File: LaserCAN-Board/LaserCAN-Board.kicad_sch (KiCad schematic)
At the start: 49 parts, among them J2 TC2050-IDC-NL, U1 NCP730BMT330TBG, U10 M24C64-RMN6TP, U2 VL53L1CXV0FY1, U4 STM32F103C8Tx, U9 SN65HVD230, U9 TPS54202DDC

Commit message: Rev 4 updates
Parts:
- removed D4, D5: PESD1CAN,215, PESD1CAN:SOT-23_L2.9-W1.3-P1.90-LS2.4-BR, symbol PESD1CAN:PESD1CAN,215
- removed R1, R5: 10k, Resistor_SMD:R_0402_1005Metric, symbol Device:R
- removed R3, R4: 4k7, Resistor_SMD:R_0402_1005Metric, symbol Device:R
- removed U1: NCP730BMT330TBG, NCP730BMT330TBG:WDFN-6_L2.0-W2.0-P0.65-BL-EP-1, symbol NCP730BMT330TBG:NCP730BMT330TBG
- added C10, C11: 22uF, Capacitor_SMD:C_0603_1608Metric, symbol Device:C_Small
- added C14, C15: 100n, Capacitor_SMD:C_0402_1005Metric, symbol Device:C_Small
- added D4: ESDCAN24-2BLY, Package_TO_SOT_SMD:SOT-23, symbol Power_Protection:SZNUP2105L
- added D6: SMF12A, Diode_SMD:D_SOD-123F, symbol Diode:SMF12A
- added NT1: NetTie_2, NetTie:NetTie-2_SMD_Pad0.5mm, symbol Device:NetTie_2
- added NT2: NetTie_2, NetTie:NetTie-2_SMD_Pad2.0mm, symbol Device:NetTie_2
- added RN1: YC164-JR-074K7L, Resistor_SMD:R_Array_Convex_4x0603, symbol Device:R_Pack04
- added U1: TPS7A2033PDBVR, Package_TO_SOT_SMD:SOT-23-5, symbol Regulator_Linear:TPS7A0508PDBV
- C19: value 22uF -> 10uF; footprint Capacitor_SMD:C_0805_2012Metric -> Capacitor_SMD:C_0603_1608Metric; LCSC Part C45783 -> C96446
- D1: value SS14 -> ZLLS400TA; footprint Diode_SMD:D_SMA -> Diode_SMD:D_SOD-323; LCSC Part C2480 -> C460267
- R9: LCSC Part C23164 -> C3009058
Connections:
- net +12V: now also D6.1 (A1)
- net +3V3: now also C19.1, C14.1, C15.1, RN1.5 (R4.2), RN1.6 (R3.2), RN1.7 (R2.2), RN1.8 (R1.2), U1.5 (OUT)
- net 3V87: now also C10.1, C11.1, U1.1 (IN), U1.3 (EN); no longer C19.1
- net CANH: now also D4.1 (K)
- net CANL: now also D4.2 (K)
- net GND: now also C10.2, C11.2, C14.2, C15.2, D4.3 (A), D6.2 (A2), NT1.2, NT2.1, U1.2 (GND); no longer J4.1, J5.1, R8.2
- net I2C_SCL: now also RN1.2 (R2.1)
- net I2C_SDA: now also RN1.1 (R1.1)
- net TOF_INT: now also RN1.3 (R3.1)
- net TOF_SHUT: now also RN1.4 (R4.1)
- new net: NT1.1, R8.2
- new net GNDPWR: J4.1, J5.1, NT2.2
- no-connect marks 34 -> 33
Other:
- note added: "CRCW06034R70JNEAHP for pulse"
- note added: "ESD Protection Diode"

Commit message: Rev 4 - more updates
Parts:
- added C20, C21: 33pF, Capacitor_SMD:C_0402_1005Metric, symbol Device:C_Small
- added Y1: 8MHz 20pF, Crystal:Crystal_SMD_3225-4Pin_3.2x2.5mm, symbol Device:Crystal_GND24_Small
- D6: value SMF12A -> SMF15CA; footprint Diode_SMD:D_SOD-123F -> Diode_SMD:D_SMF; symbol Diode:SMF12A -> Device:D_TVS; LCSC Part (none) -> C726952
- U1: LCSC Part (none) -> C2862740
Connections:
- net GND: now also C20.1, C21.1, Y1.2, Y1.4
- net at U4.5 (PD0): now also C21.2, Y1.3
- net at U4.6 (PD1): now also C20.2, Y1.1
- no-connect marks 33 -> 31
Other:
- moved on the sheet: C4, R10

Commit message: Rev 4 Complete, barring any more review
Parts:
- removed D1: ZLLS400TA, Diode_SMD:D_SOD-323, symbol Device:D_Schottky
- added D1: 12V, Diode_SMD:D_SOD-523, symbol Device:D_Zener_Small
- added Q1: Si2309CDS-T1-GE3, SI2309CDS-T1-GE3:SOT-23_L2.9-W1.3-P1.90-LS2.4-BR, symbol SI2309CDS-T1-GE3:Si2309CDS-T1-GE3
- added R1: 10k, Resistor_SMD:R_0402_1005Metric, symbol Device:R_US
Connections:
- net +12V: now also Q1.3 (D)
- net GND: now also U4.4 (PC15), R1.1
- net at R9.1: now also D1.1 (K), Q1.2 (S)
- new net: D1.2 (A), Q1.1 (G), R1.2
- no-connect marks 31 -> 30
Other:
- moved on the sheet: D6, FB1, R9

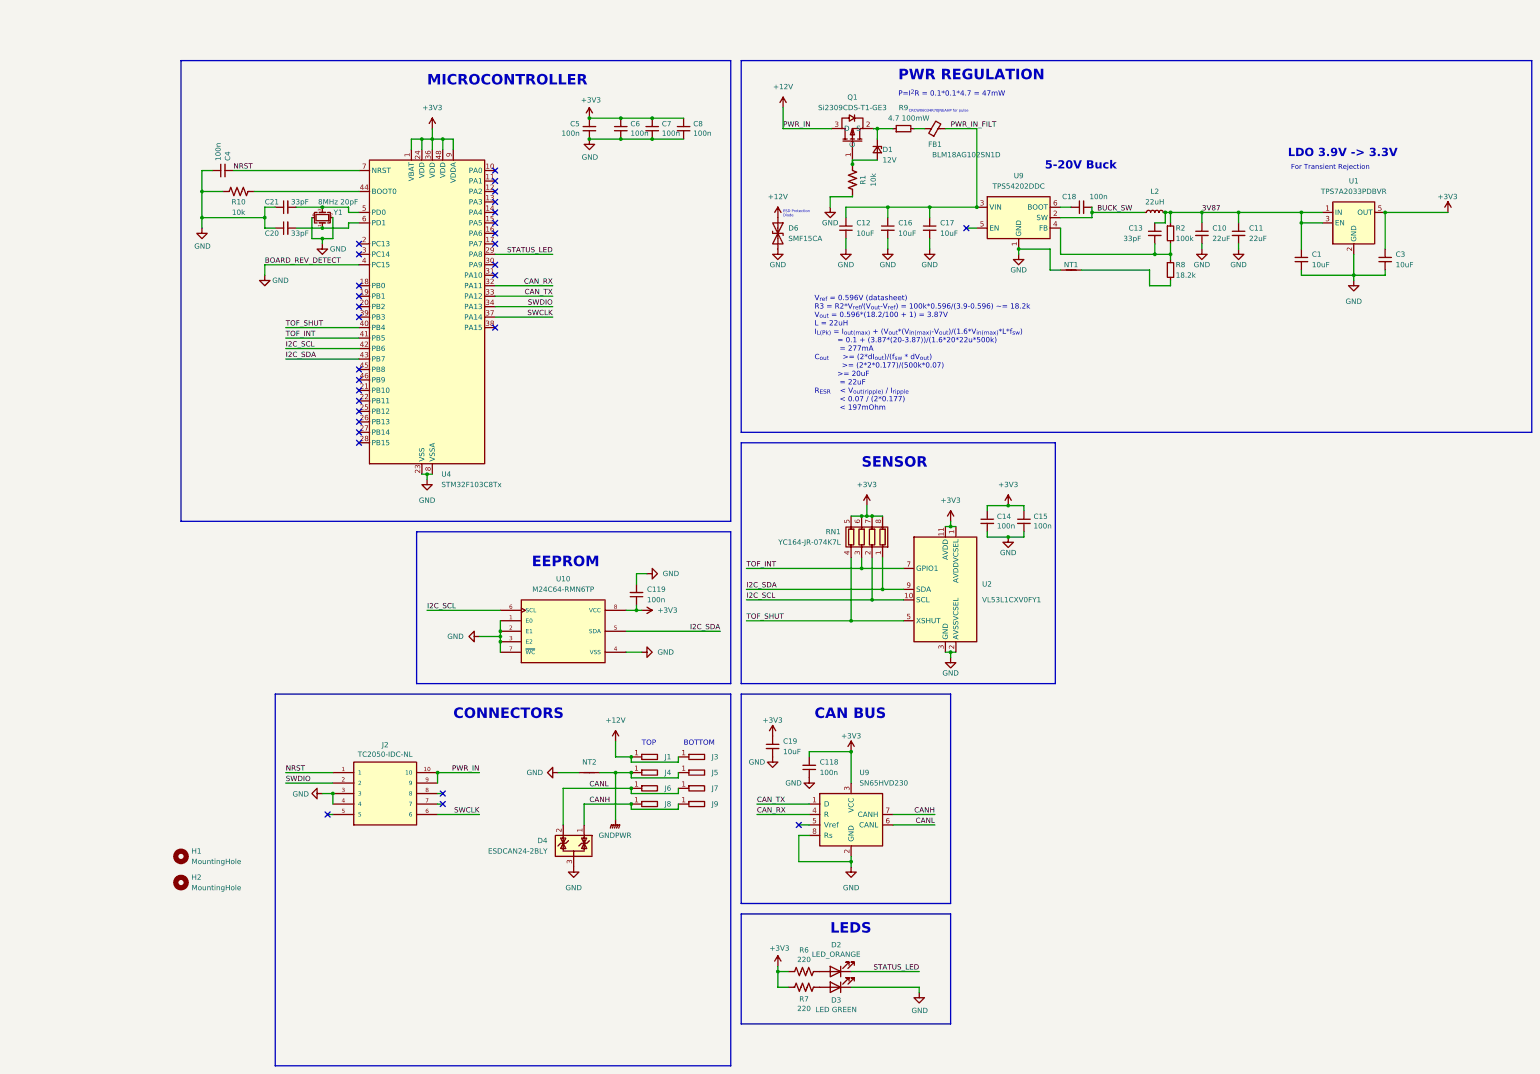
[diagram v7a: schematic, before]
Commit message: Rev 4 updates - NPTH, improved routing, BOM optimisation
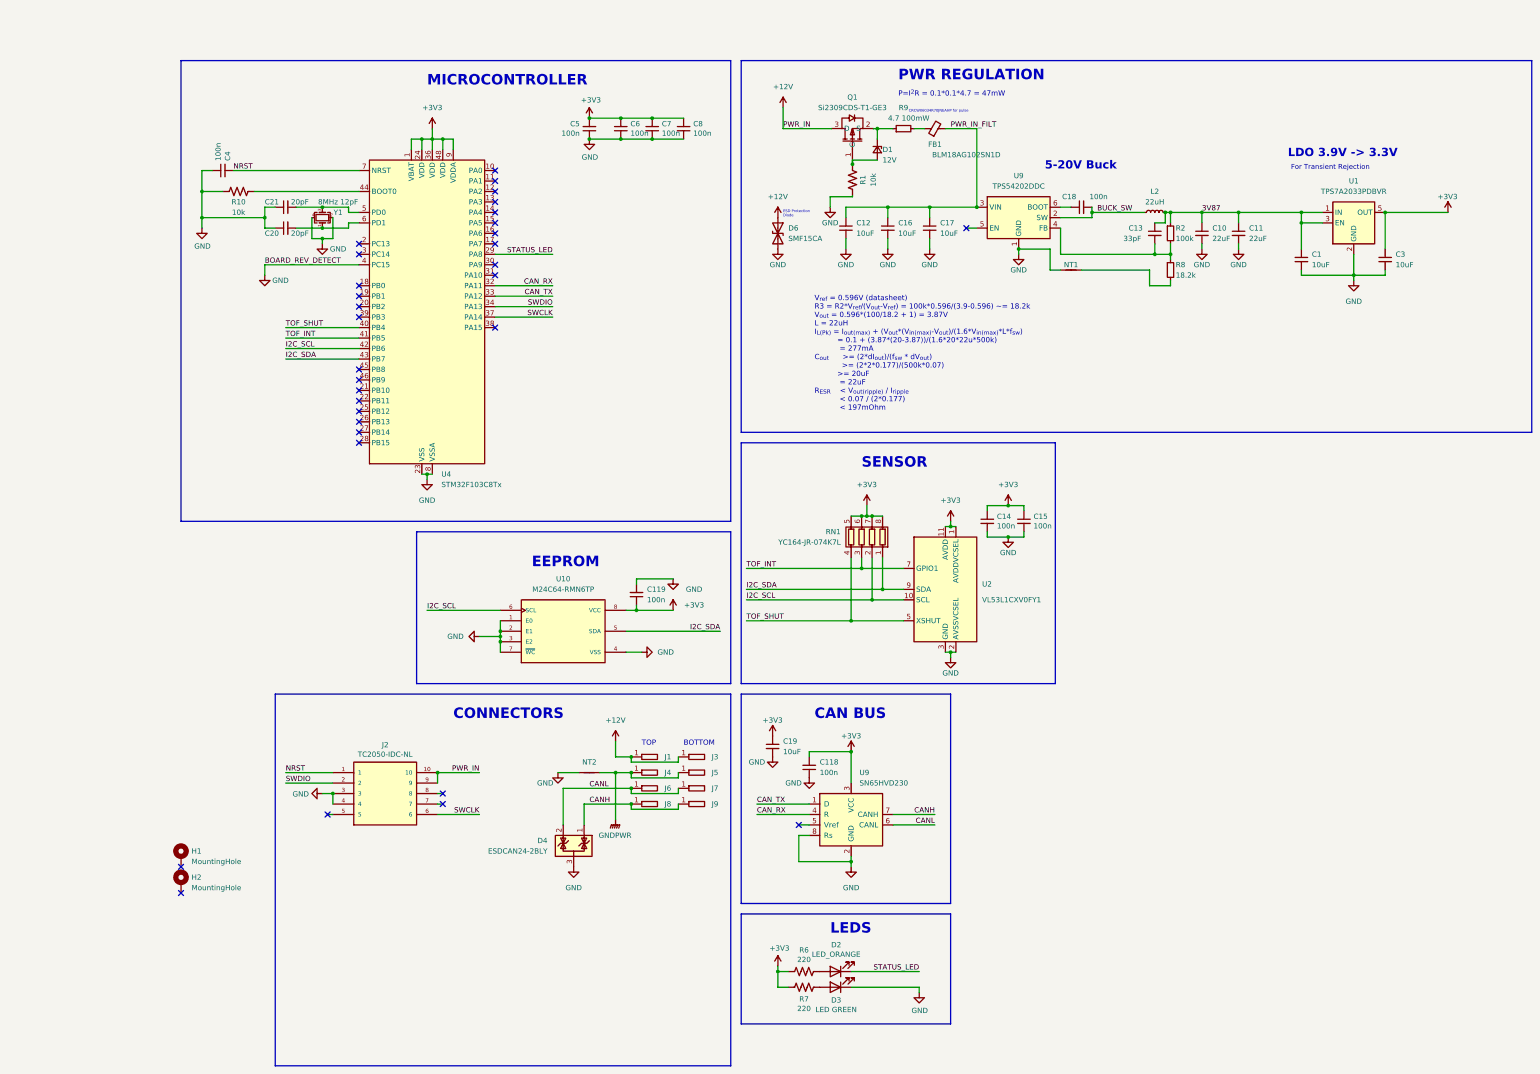
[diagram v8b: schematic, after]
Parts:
- C20, C21: value 33pF -> 20pF; LCSC Part C1562 -> C1554
- D1: LCSC C131801 -> (none); LCSC Part (none) -> C131801
- H1, H2: footprint MountingHole:MountingHole_3.2mm_M3 -> MountingHole:MountingHole_3.2mm_M3_Pad_TopBottom; symbol Mechanical:MountingHole -> Mechanical:MountingHole_Pad
- Y1: value 8MHz 20pF -> 8MHz 12pF
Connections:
- no-connect marks 30 -> 32
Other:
- note added: "V_{ref} = 0.596V (datasheet) R3 = R2*V_{ref}/(V_{out}-V_{ref}) = 100k*0.596/(3.9-0.596) ~= 18.2k V_{out} = 0.596*(100/18.2 + 1) = 3.87V L = 22uH I_{L(Pk)} = I_{out(max)} + (V_{out}*(V_{in(max)}-V_{out})/(1.6*V_{in(max)}*L*f_{sw}) = 0.1 + (3.87*(20-3.87))/(1.6*20*22u*500k) = 277mA C_{out} >= (2*dI_{out})/(f_{sw} * dV_{out}) >= (2*2*0.177)/(500k*0.07) >= 20uF = 22uF R_{ESR} < V_{out(ripple)} / I_{r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"
- note removed: "V_{ref} = 0.596V (datasheet) R3 = R2*V_{ref}/(V_{out}-V_{ref}) = 100k*0.596/(3.9-0.596) ~= 18.2k V_{out} = 0.596*(18.2/100 + 1) = 3.87V L = 22uH I_{L(Pk)} = I_{out(max)} + (V_{out}*(V_{in(max)}-V_{out})/(1.6*V_{in(max)}*L*f_{sw}) = 0.1 + (3.87*(20-3.87))/(1.6*20*22u*500k) = 277mA C_{out} >= (2*dI_{out})/(f_{sw} * dV_{out}) >= (2*2*0.177)/(500k*0.07) >= 20uF = 22uF R_{ESR} < V_{out(ripple)} / I_{r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"
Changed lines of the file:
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@@
   (no_connect (at 93.98 210.82))
   (no_connect (at 101.6 74.93))
+  (no_connect (at 58.42 223.52))
   (no_connect (at 101.6 118.11))
   (no_connect (at 134.62 92.71))
@@
   (no_connect (at 134.62 69.85))
   (no_connect (at 101.6 102.87))
+  (no_connect (at 58.42 229.87))
   (no_connect (at 101.6 120.65))
   (no_connect (at 101.6 90.17))
@@
     (stroke (width 0) (type default))
   )
-  (wire (pts (xy 168.91 152.4) (xy 168.91 154.94))
+  (wire (pts (xy 168.91 153.67) (xy 168.91 154.94))
     (stroke (width 0) (type default))
   )
@@
     (stroke (width 0) (type default))
   )
-  (wire (pts (xy 171.45 152.4) (xy 168.91 152.4))
+  (wire (pts (xy 177.8 153.67) (xy 168.91 153.67))
     (stroke (width 0) (type default))
   )
@@
     (stroke (width 0) (type default))
   )
-  (wire (pts (xy 168.91 161.29) (xy 170.18 161.29))
+  (wire (pts (xy 168.91 161.29) (xy 177.8 161.29))
     (stroke (width 0) (type default))
   )
@@
     (effects (font (size 0.635 0.635)) (justify left bottom))
   )
-  (text "V_{ref} = 0.596V (datasheet)\nR3 = R2*V_{ref}/(V_{out}-V_{ref}) = 100k*0.596/(3.9-0.596) ~= 18.2k\nV_{out} = 0.596*(18.2/100 + 1) = 3.87V\nL = 22uH\nI_{L(Pk)} = I_{out(max)} + (V_{out}*(V_{in(max)}-V_{out})/(1.6*V_{in(max)}*L*f_{sw})\n		  = 0.1 + (3.87*(20-3.87))/(1.6*20*22u*500k)\n 		  = 277mA\nC_{out}	  >= (2*dI_{out})/(f_{sw} * dV_{out})\n  		  >= (2*2*0.177)/(500k*0.07)\n		  >= 20uF\n	       = 22uF\nR_{ESR}    < V_{out(ripple)} / I_{ripple}\n		   < 0.07 / (2*0.177)\n		   < 197mOhm"
+  (text "V_{ref} = 0.596V (datasheet)\nR3 = R2*V_{ref}/(V_{out}-V_{ref}) = 100k*0.596/(3.9-0.596) ~= 18.2k\nV_{out} = 0.596*(100/18.2 + 1) = 3.87V\nL = 22uH\nI_{L(Pk)} = I_{out(max)} + (V_{out}*(V_{in(max)}-V_{out})/(1.6*V_{in(max)}*L*f_{sw})\n		  = 0.1 + (3.87*(20-3.87))/(1.6*20*22u*500k)\n 		  = 277mA\nC_{out}	  >= (2*dI_{out})/(f_{sw} * dV_{out})\n  		  >= (2*2*0.177)/(500k*0.07)\n		  >= 20uF\n	       = 22uF\nR_{ESR}    < V_{out(ripple)} / I_{ripple}\n		   < 0.07 / (2*0.177)\n		   < 197mOhm"
     (at 212.09 113.03 0)
     (effects (font (size 1.27 1.27)) (justify left bottom))
@@
     )
   )
-  (symbol (lib_id "power:GND") (at 171.45 152.4 90) (unit 1)
-    (in_bom yes) (on_board yes) (dnp no) (fields_autoplaced)
-    (property "Reference" "#PWR0198" (at 177.8 152.4 0)
+  (symbol (lib_id "power:GND") (at 177.8 153.67 0) (unit 1)
+    (in_bom yes) (on_board yes) (dnp no)
+    (property "Reference" "#PWR0198" (at 177.8 160.02 0)
       (effects (font (size 1.27 1.27)) hide)
     )
-    (property "Value" "GND" (at 175.26 152.3999 90)
-      (effects (font (size 1.27 1.27)) (justify right))
+    (property "Value" "GND" (at 182.88 156.21 0)
+      (effects (font (size 1.27 1.27)))
     )
-    (property "Footprint" "" (at 171.45 152.4 0)
+    (property "Footprint" "" (at 177.8 153.67 0)
       (effects (font (size 1.27 1.27)) hide)
     )
-    (property "Datasheet" "" (at 171.45 152.4 0)
+    (property "Datasheet" "" (at 177.8 153.67 0)
       (effects (font (size 1.27 1.27)) hide)
     )
@@
     )
   )
-  (symbol (lib_id "power:+3V3") (at 170.18 161.29 270) (unit 1)
-    (in_bom yes) (on_board yes) (dnp no) (fields_autoplaced)
-    (property "Reference" "#PWR0196" (at 166.37 161.29 0)
+  (symbol (lib_id "power:+3V3") (at 177.8 161.29 0) (unit 1)
+    (in_bom yes) (on_board yes) (dnp no)
+    (property "Reference" "#PWR0196" (at 177.8 165.1 0)
       (effects (font (size 1.27 1.27)) hide)
     )
-    (property "Value" "+3V3" (at 173.99 161.2899 90)
-      (effects (font (size 1.27 1.27)) (justify left))
+    (property "Value" "+3V3" (at 182.88 160.02 0)
+      (effects (font (size 1.27 1.27)))
     )
-    (property "Footprint" "" (at 170.18 161.29 0)
+    (property "Footprint" "" (at 177.8 161.29 0)
       (effects (font (size 1.27 1.27)) hide)
     )
-    (property "Datasheet" "" (at 170.18 161.29 0)
+    (property "Datasheet" "" (at 177.8 161.29 0)
       (effects (font (size 1.27 1.27)) hide)
     )
@@
       (effects (font (size 1.27 1.27)))
     )
-    (property "Value" "8MHz 20pF" (at 96.52 62.23 90)
+    (property "Value" "8MHz 12pF" (at 96.52 62.23 90)
       (effects (font (size 1.27 1.27)))
     )
@@
       (effects (font (size 1.27 1.27)) (justify right))
     )
-    (property "Value" "33pF" (at 85.09 62.23 90)
+    (property "Value" "20pF" (at 85.09 62.23 90)
       (effects (font (size 1.27 1.27)) (justify right))
     )
@@
       (effects (font (size 1.27 1.27)) hide)
     )
-    (property "LCSC Part" "C1562" (at 83.82 63.5 0)
+    (property "LCSC Part" "C1554" (at 83.82 63.5 0)
       (effects (font (size 1.27 1.27)) hide)
     )
@@
       (effects (font (size 1.27 1.27)) (justify right))
     )
-    (property "Value" "33pF" (at 85.09 69.85 90)
+    (property "Value" "20pF" (at 85.09 69.85 90)
       (effects (font (size 1.27 1.27)) (justify right))
     )
@@
       (effects (font (size 1.27 1.27)) hide)
     )
-    (property "LCSC Part" "C1562" (at 83.82 68.58 0)
+    (property "LCSC Part" "C1554" (at 83.82 68.58 0)
       (effects (font (size 1.27 1.27)) hide)
     )
@@
     )
   )
-  (symbol (lib_id "Mechanical:MountingHole") (at 58.42 220.98 0) (unit 1)
+  (symbol (lib_id "Mechanical:MountingHole_Pad") (at 58.42 220.98 0) (unit 1)
     (in_bom no) (on_board yes) (dnp no) (fields_autoplaced)
     (property "Reference" "H1" (at 60.96 219.7099 0)
@@
       (effects (font (size 1.27 1.27)) (justify left))
     )
-    (property "Footprint" "MountingHole:MountingHole_3.2mm_M3" (at 58.42 220.98 0)
+    (property "Footprint" "MountingHole:MountingHole_3.2mm_M3_Pad_TopBottom" (at 58.42 220.98 0)
       (effects (font (size 1.27 1.27)) hide)
     )
@@
       (effects (font (size 1.27 1.27)) hide)
     )
+    (pin "1")
     (instances
       (project "LaserCAN-Board"
@@
       (effects (font (size 1.27 1.27)) hide)
     )
-    (property "LCSC" "C131801" (at 227.33 49.53 90)
+    (property "LCSC Part" "C131801" (at 227.33 49.53 90)
       (effects (font (size 1.27 1.27)) hide)
     )
@@
     )
   )
-  (symbol (lib_id "Mechanical:MountingHole") (at 58.42 227.33 0) (unit 1)
+  (symbol (lib_id "Mechanical:MountingHole_Pad") (at 58.42 227.33 0) (unit 1)
     (in_bom no) (on_board yes) (dnp no) (fields_autoplaced)
     (property "Reference" "H2" (at 60.96 226.0599 0)
@@
       (effects (font (size 1.27 1.27)) (justify left))
     )
-    (property "Footprint" "MountingHole:MountingHole_3.2mm_M3" (at 58.42 227.33 0)
+    (property "Footprint" "MountingHole:MountingHole_3.2mm_M3_Pad_TopBottom" (at 58.42 227.33 0)
       (effects (font (size 1.27 1.27)) hide)
     )
@@
       (effects (font (size 1.27 1.27)) hide)
     )
+    (pin "1")
     (instances
       (project "LaserCAN-Board"
@@
     )
   )
-  (symbol (lib_id "power:GND") (at 149.86 200.66 270) (unit 1)
+  (symbol (lib_id "power:GND") (at 149.86 200.66 0) (unit 1)
     (in_bom yes) (on_board yes) (dnp no)
-    (property "Reference" "#PWR0121" (at 143.51 200.66 0)
+    (property "Reference" "#PWR0121" (at 149.86 207.01 0)
       (effects (font (size 1.27 1.27)) hide)
     )
-    (property "Value" "GND" (at 142.24 200.66 90)
+    (property "Value" "GND" (at 144.78 203.2 0)
       (effects (font (size 1.27 1.27)) (justify left))
     )
